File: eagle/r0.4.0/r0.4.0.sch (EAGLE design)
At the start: 8 parts

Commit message: Added finishing touches to r0.4.0 of the board
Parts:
- removed JP1: (no value), pinhead:PINHD-2X2
- added USB: value?, pinhead:PINHD-2X2
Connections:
- new net N$4: 12VDC_AND_LED.B-1, 12VDC_AND_LED.B-6, RF_HEADER1.1, RF_HEADER1.3, RF_HEADER1.5, RF_HEADER1.7, U$1.GND, USB.1, X_TILT.2
- new net N$7: 12VDC_AND_LED.B-5, U$1.*5
- net N$11: now also 12VDC_AND_LED.B-4, U$1.*6; no longer 12VDC_AND_LED.B-1, 12VDC_AND_LED.B-6, JP1.2, RF_HEADER1.1, RF_HEADER1.3, RF_HEADER1.5, RF_HEADER1.7, U$1.GND, X_TILT.2
- net N$9: now also USB.3; no longer JP1.4
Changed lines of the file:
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@@
 <part name="RF_HEADER1" library="rf-header" deviceset="PINHD-2X4" device="" value="value?"/>
 <part name="12VDC_AND_LED" library="con-wago" deviceset="234-206" device="" value="value?"/>
-<part name="JP1" library="pinhead" deviceset="PINHD-2X2" device=""/>
+<part name="USB" library="pinhead" deviceset="PINHD-2X2" device="" value="value?"/>
 </parts>
 <sheets>
@@
 <instance part="RF_HEADER1" gate="A" x="5.08" y="17.78"/>
 <instance part="12VDC_AND_LED" gate="G$1" x="-76.2" y="-15.24" rot="R180"/>
-<instance part="JP1" gate="A" x="-66.04" y="-33.02"/>
+<instance part="USB" gate="A" x="-20.32" y="-33.02"/>
 </instances>
 <busses>
@@
 <junction x="-43.18" y="-17.78"/>
 <pinref part="12VDC_AND_LED" gate="G$1" pin="B-2"/>
+<pinref part="12VDC_AND_LED" gate="G$1" pin="B-3"/>
 <wire x1="-43.18" y1="-17.78" x2="-68.58" y2="-17.78" width="0.1524" layer="91"/>
-<pinref part="12VDC_AND_LED" gate="G$1" pin="B-3"/>
 <wire x1="-68.58" y1="-15.24" x2="-43.18" y2="-15.24" width="0.1524" layer="91"/>
-<pinref part="JP1" gate="A" pin="4"/>
-<wire x1="-63.5" y1="-33.02" x2="-43.18" y2="-33.02" width="0.1524" layer="91"/>
-<wire x1="-43.18" y1="-33.02" x2="-43.18" y2="-17.78" width="0.1524" layer="91"/>
+<junction x="-43.18" y="-17.78"/>
+<wire x1="-43.18" y1="-17.78" x2="-43.18" y2="-33.02" width="0.1524" layer="91"/>
+<pinref part="USB" gate="A" pin="3"/>
+<wire x1="-43.18" y1="-33.02" x2="-25.4" y2="-33.02" width="0.1524" layer="91"/>
 </segment>
 </net>
@@
 </segment>
 </net>
-<net name="N$11" class="0">
+<net name="N$12" class="0">
+<segment>
+<pinref part="U$1" gate="G$1" pin="A4"/>
+<wire x1="-2.54" y1="40.64" x2="-7.62" y2="40.64" width="0.1524" layer="91"/>
+<wire x1="-7.62" y1="40.64" x2="-7.62" y2="33.02" width="0.1524" layer="91"/>
+<wire x1="-7.62" y1="33.02" x2="20.32" y2="33.02" width="0.1524" layer="91"/>
+<wire x1="20.32" y1="33.02" x2="20.32" y2="20.32" width="0.1524" layer="91"/>
+<pinref part="RF_HEADER1" gate="A" pin="4"/>
+<wire x1="20.32" y1="20.32" x2="10.16" y2="20.32" width="0.1524" layer="91"/>
+</segment>
+</net>
+<net name="N$18" class="0">
+<segment>
+<pinref part="U$1" gate="G$1" pin="A5"/>
+<wire x1="-2.54" y1="38.1" x2="-5.08" y2="38.1" width="0.1524" layer="91"/>
+<wire x1="-5.08" y1="38.1" x2="-5.08" y2="30.48" width="0.1524" layer="91"/>
+<wire x1="-5.08" y1="30.48" x2="17.78" y2="30.48" width="0.1524" layer="91"/>
+<wire x1="17.78" y1="30.48" x2="17.78" y2="22.86" width="0.1524" layer="91"/>
+<pinref part="RF_HEADER1" gate="A" pin="2"/>
+<wire x1="17.78" y1="22.86" x2="10.16" y2="22.86" width="0.1524" layer="91"/>
+</segment>
+</net>
+<net name="N$19" class="0">
+<segment>
+<pinref part="U$1" gate="G$1" pin="A6"/>
+<wire x1="20.32" y1="38.1" x2="22.86" y2="38.1" width="0.1524" layer="91"/>
+<wire x1="22.86" y1="38.1" x2="22.86" y2="15.24" width="0.1524" layer="91"/>
+<pinref part="RF_HEADER1" gate="A" pin="8"/>
+<wire x1="22.86" y1="15.24" x2="10.16" y2="15.24" width="0.1524" layer="91"/>
+</segment>
+</net>
+<net name="N$20" class="0">
+<segment>
+<pinref part="U$1" gate="G$1" pin="A7"/>
+<wire x1="20.32" y1="40.64" x2="25.4" y2="40.64" width="0.1524" layer="91"/>
+<wire x1="25.4" y1="40.64" x2="25.4" y2="17.78" width="0.1524" layer="91"/>
+<pinref part="RF_HEADER1" gate="A" pin="6"/>
+<wire x1="25.4" y1="17.78" x2="10.16" y2="17.78" width="0.1524" layer="91"/>
+</segment>
+</net>
+<net name="N$4" class="0">
 <segment>
 <pinref part="RF_HEADER1" gate="A" pin="1"/>
@@
 <wire x1="-33.02" y1="22.86" x2="-33.02" y2="-7.62" width="0.1524" layer="91"/>
 <wire x1="-33.02" y1="-7.62" x2="-33.02" y2="-20.32" width="0.1524" layer="91"/>
-<wire x1="-33.02" y1="-20.32" x2="-33.02" y2="-30.48" width="0.1524" layer="91"/>
 <pinref part="U$1" gate="G$1" pin="GND"/>
 <wire x1="-33.02" y1="66.04" x2="-2.54" y2="66.04" width="0.1524" layer="91"/>
@@
 <pinref part="12VDC_AND_LED" gate="G$1" pin="B-1"/>
 <wire x1="-68.58" y1="-20.32" x2="-33.02" y2="-20.32" width="0.1524" layer="91"/>
-<junction x="-33.02" y="-20.32"/>
-<pinref part="JP1" gate="A" pin="2"/>
-<wire x1="-63.5" y1="-30.48" x2="-33.02" y2="-30.48" width="0.1524" layer="91"/>
 <pinref part="12VDC_AND_LED" gate="G$1" pin="B-6"/>
 <wire x1="-68.58" y1="-7.62" x2="-33.02" y2="-7.62" width="0.1524" layer="91"/>
 <junction x="-33.02" y="-7.62"/>
-</segment>
-</net>
-<net name="N$12" class="0">
-<segment>
-<pinref part="U$1" gate="G$1" pin="A4"/>
-<wire x1="-2.54" y1="40.64" x2="-7.62" y2="40.64" width="0.1524" layer="91"/>
-<wire x1="-7.62" y1="40.64" x2="-7.62" y2="33.02" width="0.1524" layer="91"/>
-<wire x1="-7.62" y1="33.02" x2="20.32" y2="33.02" width="0.1524" layer="91"/>
-<wire x1="20.32" y1="33.02" x2="20.32" y2="20.32" width="0.1524" layer="91"/>
-<pinref part="RF_HEADER1" gate="A" pin="4"/>
-<wire x1="20.32" y1="20.32" x2="10.16" y2="20.32" width="0.1524" layer="91"/>
-</segment>
-</net>
-<net name="N$18" class="0">
-<segment>
-<pinref part="U$1" gate="G$1" pin="A5"/>
-<wire x1="-2.54" y1="38.1" x2="-5.08" y2="38.1" width="0.1524" layer="91"/>
-<wire x1="-5.08" y1="38.1" x2="-5.08" y2="30.48" width="0.1524" layer="91"/>
-<wire x1="-5.08" y1="30.48" x2="17.78" y2="30.48" width="0.1524" layer="91"/>
-<wire x1="17.78" y1="30.48" x2="17.78" y2="22.86" width="0.1524" layer="91"/>
-<pinref part="RF_HEADER1" gate="A" pin="2"/>
-<wire x1="17.78" y1="22.86" x2="10.16" y2="22.86" width="0.1524" layer="91"/>
-</segment>
-</net>
-<net name="N$19" class="0">
-<segment>
-<pinref part="U$1" gate="G$1" pin="A6"/>
-<wire x1="20.32" y1="38.1" x2="22.86" y2="38.1" width="0.1524" layer="91"/>
-<wire x1="22.86" y1="38.1" x2="22.86" y2="15.24" width="0.1524" layer="91"/>
-<pinref part="RF_HEADER1" gate="A" pin="8"/>
-<wire x1="22.86" y1="15.24" x2="10.16" y2="15.24" width="0.1524" layer="91"/>
-</segment>
-</net>
-<net name="N$20" class="0">
-<segment>
-<pinref part="U$1" gate="G$1" pin="A7"/>
-<wire x1="20.32" y1="40.64" x2="25.4" y2="40.64" width="0.1524" layer="91"/>
-<wire x1="25.4" y1="40.64" x2="25.4" y2="17.78" width="0.1524" layer="91"/>
-<pinref part="RF_HEADER1" gate="A" pin="6"/>
-<wire x1="25.4" y1="17.78" x2="10.16" y2="17.78" width="0.1524" layer="91"/>
-</segment>
-</net>
+<pinref part="USB" gate="A" pin="1"/>
+<wire x1="-25.4" y1="-30.48" x2="-33.02" y2="-30.48" width="0.1524" layer="91"/>
+<wire x1="-33.02" y1="-30.48" x2="-33.02" y2="-20.32" width="0.1524" layer="91"/>
+<junction x="-33.02" y="-20.32"/>
+</segment>
+</net>
+<net name="N$7" class="0">
+<segment>
+<pinref part="U$1" gate="G$1" pin="*5"/>
+<wire x1="-2.54" y1="55.88" x2="-38.1" y2="55.88" width="0.1524" layer="91"/>
+<wire x1="-38.1" y1="55.88" x2="-38.1" y2="-10.16" width="0.1524" layer="91"/>
+<pinref part="12VDC_AND_LED" gate="G$1" pin="B-5"/>
+<wire x1="-38.1" y1="-10.16" x2="-68.58" y2="-10.16" width="0.1524" layer="91"/>
+</segment>
+</net>
+<net name="N$11" class="0">
+<segment>
+<pinref part="12VDC_AND_LED" gate="G$1" pin="B-4"/>
+<wire x1="-35.56" y1="-12.7" x2="-68.58" y2="-12.7" width="0.1524" layer="91"/>
+<pinref part="U$1" gate="G$1" pin="*6"/>
+<wire x1="-2.54" y1="53.34" x2="-35.56" y2="53.34" width="0.1524" layer="91"/>
+<wire x1="-35.56" y1="-12.7" x2="-35.56" y2="53.34" width="0.1524" layer="91"/>
+</segment>
+</net>

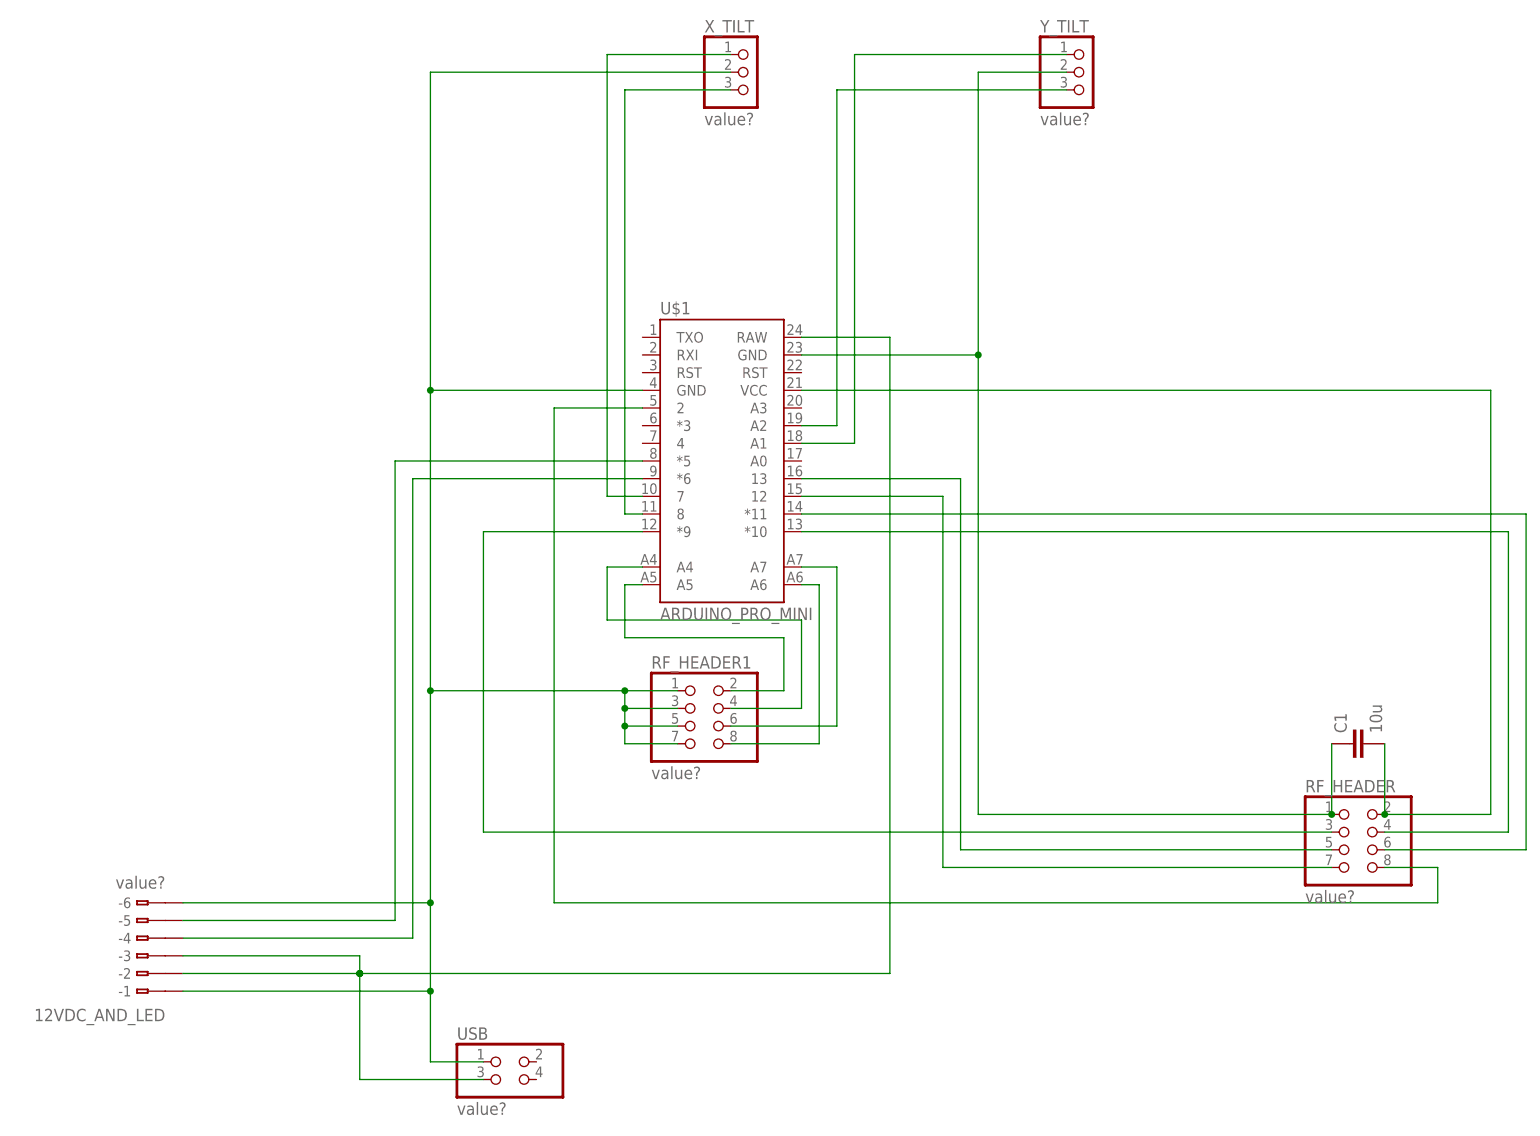
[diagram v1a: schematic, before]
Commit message: Updated r0.4.0 of the board: * Thickened usb header pads * Added a couple of pads for unused pins
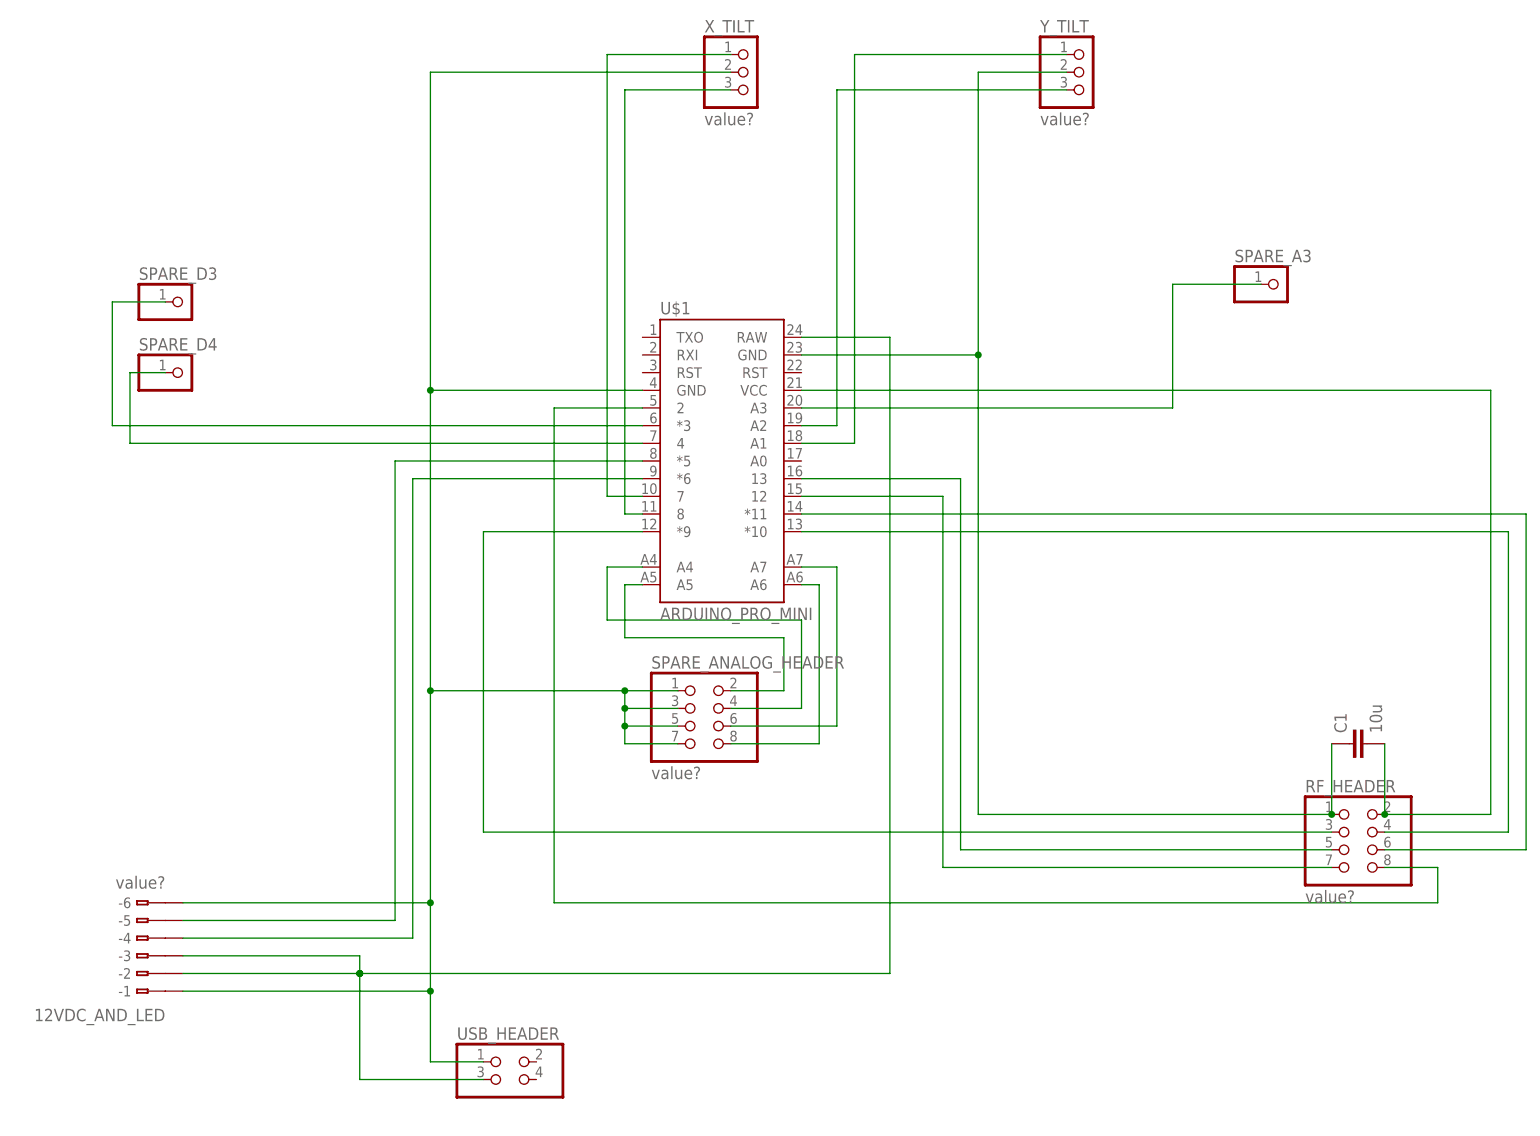
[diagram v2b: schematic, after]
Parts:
- removed USB: value?, pinhead:PINHD-2X2
- added SPARE_A3, SPARE_D3, SPARE_D4: (no value), pinhead:PINHD-1X1
- added USB_HEADER: (no value), usb-header:PINHD-2X2
- renumbered RF_HEADER1 to SPARE_ANALOG_HEADER
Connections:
- new net N$28: SPARE_A3.1, U$1.A3
- new net N$29: SPARE_D3.1, U$1.*3
- new net N$30: SPARE_D4.1, U$1.4
- net N$4: now also USB_HEADER.1; no longer USB.1
- net N$9: now also USB_HEADER.3; no longer USB.3
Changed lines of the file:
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@@
 <part name="C1" library="SparkFun-Passives" deviceset="CAP" device="PTH" value="10u"/>
 <part name="RF_HEADER" library="rf-header" deviceset="PINHD-2X4" device="" value="value?"/>
-<part name="RF_HEADER1" library="rf-header" deviceset="PINHD-2X4" device="" value="value?"/>
+<part name="SPARE_ANALOG_HEADER" library="rf-header" deviceset="PINHD-2X4" device="" value="value?"/>
 <part name="12VDC_AND_LED" library="con-wago" deviceset="234-206" device="" value="value?"/>
-<part name="USB" library="pinhead" deviceset="PINHD-2X2" device="" value="value?"/>
+<part name="SPARE_A3" library="pinhead" deviceset="PINHD-1X1" device=""/>
+<part name="SPARE_D3" library="pinhead" deviceset="PINHD-1X1" device=""/>
+<part name="SPARE_D4" library="pinhead" deviceset="PINHD-1X1" device=""/>
+<part name="USB_HEADER" library="usb-header" deviceset="PINHD-2X2" device=""/>
 </parts>
 <sheets>
@@
 <instance part="C1" gate="G$1" x="101.6" y="15.24" rot="R90"/>
 <instance part="RF_HEADER" gate="A" x="99.06" y="0"/>
-<instance part="RF_HEADER1" gate="A" x="5.08" y="17.78"/>
+<instance part="SPARE_ANALOG_HEADER" gate="A" x="5.08" y="17.78"/>
 <instance part="12VDC_AND_LED" gate="G$1" x="-76.2" y="-15.24" rot="R180"/>
-<instance part="USB" gate="A" x="-20.32" y="-33.02"/>
+<instance part="SPARE_A3" gate="G$1" x="88.9" y="81.28"/>
+<instance part="SPARE_D3" gate="G$1" x="-68.58" y="78.74"/>
+<instance part="SPARE_D4" gate="G$1" x="-68.58" y="68.58"/>
+<instance part="USB_HEADER" gate="A" x="-20.32" y="-33.02"/>
 </instances>
 <busses>
@@
 <junction x="-43.18" y="-17.78"/>
 <wire x1="-43.18" y1="-17.78" x2="-43.18" y2="-33.02" width="0.1524" layer="91"/>
-<pinref part="USB" gate="A" pin="3"/>
 <wire x1="-43.18" y1="-33.02" x2="-25.4" y2="-33.02" width="0.1524" layer="91"/>
+<pinref part="USB_HEADER" gate="A" pin="3"/>
 </segment>
 </net>
@@
 <wire x1="-7.62" y1="33.02" x2="20.32" y2="33.02" width="0.1524" layer="91"/>
 <wire x1="20.32" y1="33.02" x2="20.32" y2="20.32" width="0.1524" layer="91"/>
-<pinref part="RF_HEADER1" gate="A" pin="4"/>
+<pinref part="SPARE_ANALOG_HEADER" gate="A" pin="4"/>
 <wire x1="20.32" y1="20.32" x2="10.16" y2="20.32" width="0.1524" layer="91"/>
 </segment>
@@
 <wire x1="-5.08" y1="30.48" x2="17.78" y2="30.48" width="0.1524" layer="91"/>
 <wire x1="17.78" y1="30.48" x2="17.78" y2="22.86" width="0.1524" layer="91"/>
-<pinref part="RF_HEADER1" gate="A" pin="2"/>
+<pinref part="SPARE_ANALOG_HEADER" gate="A" pin="2"/>
 <wire x1="17.78" y1="22.86" x2="10.16" y2="22.86" width="0.1524" layer="91"/>
 </segment>
@@
 <wire x1="20.32" y1="38.1" x2="22.86" y2="38.1" width="0.1524" layer="91"/>
 <wire x1="22.86" y1="38.1" x2="22.86" y2="15.24" width="0.1524" layer="91"/>
-<pinref part="RF_HEADER1" gate="A" pin="8"/>
+<pinref part="SPARE_ANALOG_HEADER" gate="A" pin="8"/>
 <wire x1="22.86" y1="15.24" x2="10.16" y2="15.24" width="0.1524" layer="91"/>
 </segment>
@@
 <wire x1="20.32" y1="40.64" x2="25.4" y2="40.64" width="0.1524" layer="91"/>
 <wire x1="25.4" y1="40.64" x2="25.4" y2="17.78" width="0.1524" layer="91"/>
-<pinref part="RF_HEADER1" gate="A" pin="6"/>
+<pinref part="SPARE_ANALOG_HEADER" gate="A" pin="6"/>
 <wire x1="25.4" y1="17.78" x2="10.16" y2="17.78" width="0.1524" layer="91"/>
 </segment>
@@
 <net name="N$4" class="0">
 <segment>
-<pinref part="RF_HEADER1" gate="A" pin="1"/>
+<pinref part="SPARE_ANALOG_HEADER" gate="A" pin="1"/>
 <wire x1="2.54" y1="22.86" x2="-5.08" y2="22.86" width="0.1524" layer="91"/>
 <wire x1="-5.08" y1="22.86" x2="-5.08" y2="20.32" width="0.1524" layer="91"/>
-<pinref part="RF_HEADER1" gate="A" pin="7"/>
+<pinref part="SPARE_ANALOG_HEADER" gate="A" pin="7"/>
 <wire x1="-5.08" y1="20.32" x2="-5.08" y2="17.78" width="0.1524" layer="91"/>
 <wire x1="-5.08" y1="17.78" x2="-5.08" y2="15.24" width="0.1524" layer="91"/>
 <wire x1="-5.08" y1="15.24" x2="2.54" y2="15.24" width="0.1524" layer="91"/>
-<pinref part="RF_HEADER1" gate="A" pin="3"/>
+<pinref part="SPARE_ANALOG_HEADER" gate="A" pin="3"/>
 <wire x1="2.54" y1="20.32" x2="-5.08" y2="20.32" width="0.1524" layer="91"/>
 <junction x="-5.08" y="20.32"/>
-<pinref part="RF_HEADER1" gate="A" pin="5"/>
+<pinref part="SPARE_ANALOG_HEADER" gate="A" pin="5"/>
 <wire x1="2.54" y1="17.78" x2="-5.08" y2="17.78" width="0.1524" layer="91"/>
 <junction x="-5.08" y="17.78"/>
@@
 <wire x1="-68.58" y1="-7.62" x2="-33.02" y2="-7.62" width="0.1524" layer="91"/>
 <junction x="-33.02" y="-7.62"/>
-<pinref part="USB" gate="A" pin="1"/>
 <wire x1="-25.4" y1="-30.48" x2="-33.02" y2="-30.48" width="0.1524" layer="91"/>
 <wire x1="-33.02" y1="-30.48" x2="-33.02" y2="-20.32" width="0.1524" layer="91"/>
 <junction x="-33.02" y="-20.32"/>
+<pinref part="USB_HEADER" gate="A" pin="1"/>
 </segment>
 </net>
@@
 </segment>
 </net>
+<net name="N$28" class="0">
+<segment>
+<pinref part="SPARE_A3" gate="G$1" pin="1"/>
+<wire x1="86.36" y1="81.28" x2="73.66" y2="81.28" width="0.1524" layer="91"/>
+<wire x1="73.66" y1="81.28" x2="73.66" y2="63.5" width="0.1524" layer="91"/>
+<pinref part="U$1" gate="G$1" pin="A3"/>
+<wire x1="73.66" y1="63.5" x2="20.32" y2="63.5" width="0.1524" layer="91"/>
+</segment>
+</net>
+<net name="N$29" class="0">
+<segment>
+<pinref part="SPARE_D3" gate="G$1" pin="1"/>
+<wire x1="-71.12" y1="78.74" x2="-78.74" y2="78.74" width="0.1524" layer="91"/>
+<wire x1="-78.74" y1="78.74" x2="-78.74" y2="60.96" width="0.1524" layer="91"/>
+<pinref part="U$1" gate="G$1" pin="*3"/>
+<wire x1="-78.74" y1="60.96" x2="-2.54" y2="60.96" width="0.1524" layer="91"/>
+</segment>
+</net>
+<net name="N$30" class="0">
+<segment>
+<pinref part="SPARE_D4" gate="G$1" pin="1"/>
+<wire x1="-71.12" y1="68.58" x2="-76.2" y2="68.58" width="0.1524" layer="91"/>
+<wire x1="-76.2" y1="68.58" x2="-76.2" y2="58.42" width="0.1524" layer="91"/>
+<pinref part="U$1" gate="G$1" pin="4"/>
+<wire x1="-76.2" y1="58.42" x2="-2.54" y2="58.42" width="0.1524" layer="91"/>
+</segment>
+</net>
